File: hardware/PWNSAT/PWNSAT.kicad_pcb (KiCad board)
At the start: 2 copper layers, 83 x 83 mm, 137 parts, among them J1 Conn_01x03, J2 Conn_01x04_Pin, J3 Battery, J4 USB_A, J5 USB_A, P1 USB_C_Plug_USB2.0, Q1 DMG3415U-7, SW1 SW_Push, SW2 SW_Push, SW3 ON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

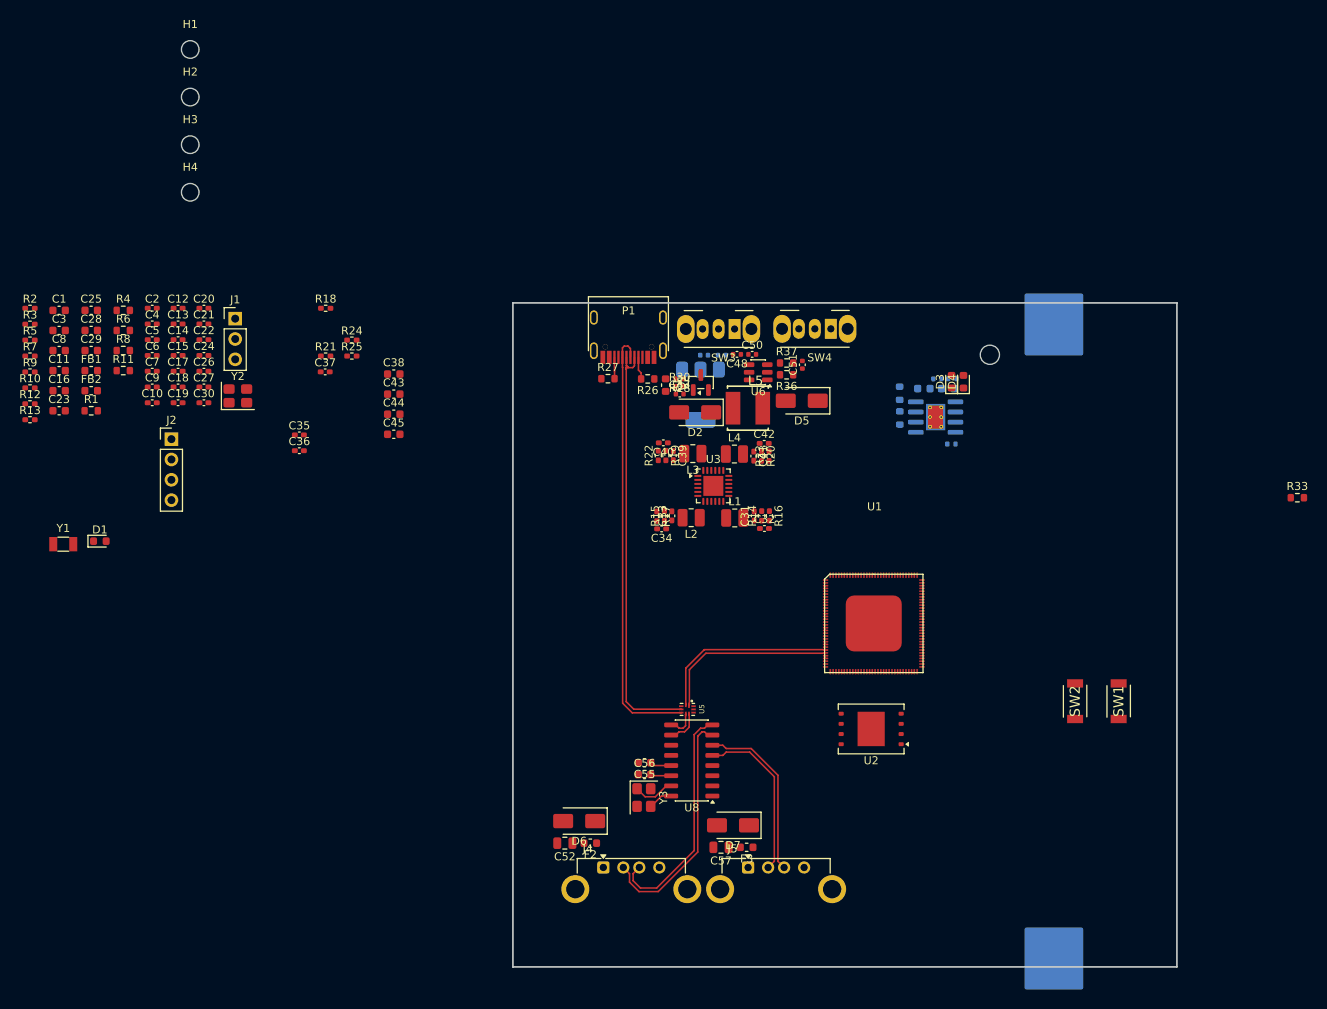
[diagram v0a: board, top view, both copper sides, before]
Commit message: feat(Hw):Update_Floorplan_Init_First _route
Pending_Battery_Type
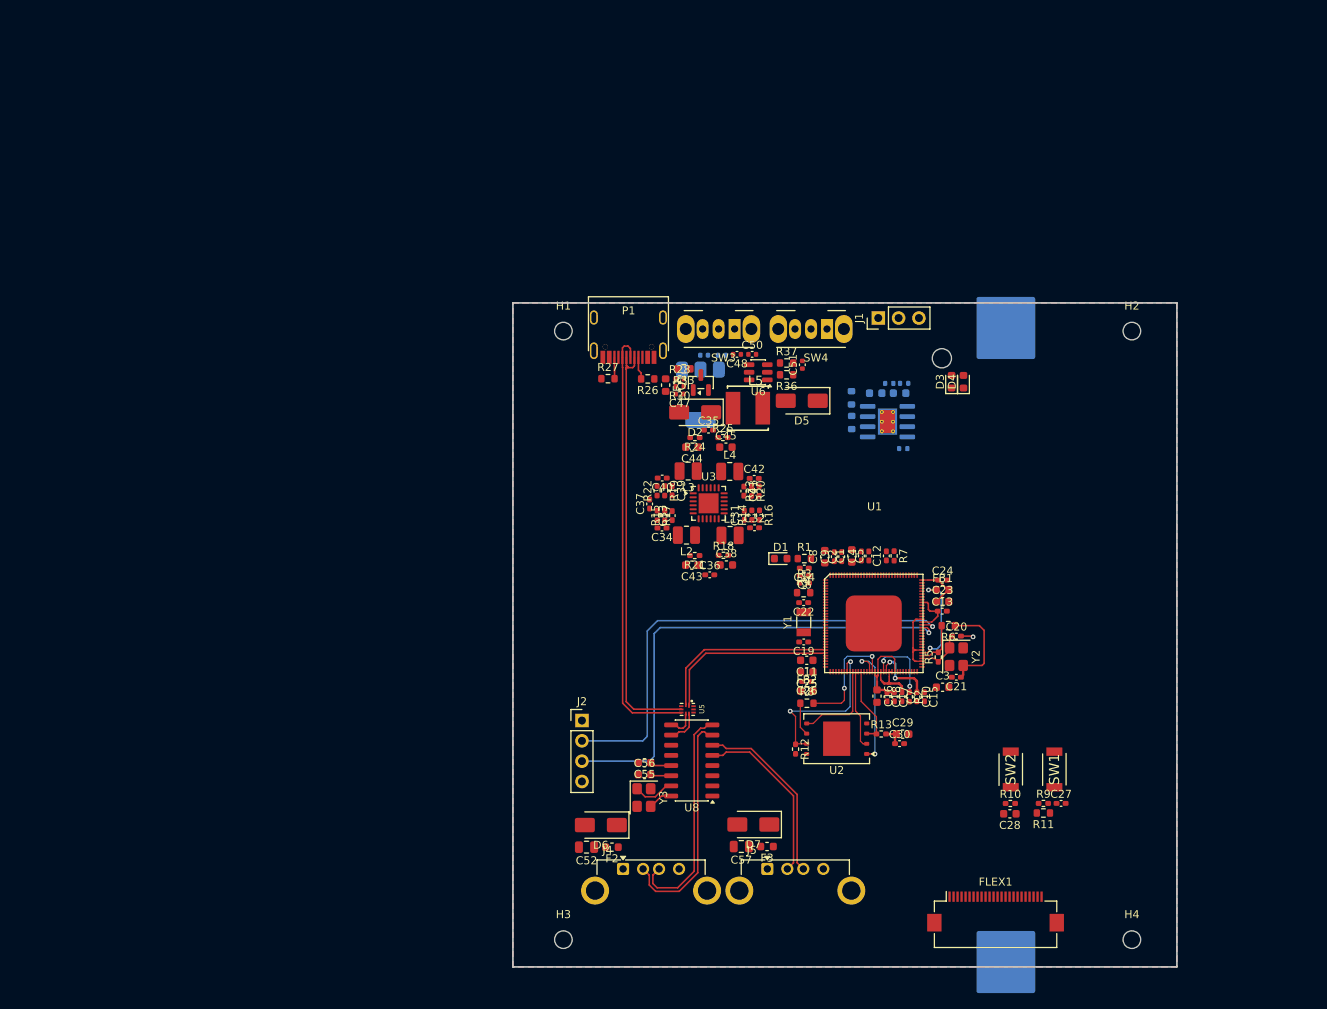
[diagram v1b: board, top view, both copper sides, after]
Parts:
- added FLEX1: FH12-24S-0.5SH(55), Connector_FFC-FPC:Hirose_FH12-24S-0.5SH_1x24-1MP_P0.50mm_Horizontal, F.Cu at (80.3, 94.2)
- moved H4 150.3 mm to (97.3, 97.7)
- moved R9 137.7 mm to (86.3, 80.7)
- moved R10 133.1 mm to (82.1, 80.7)
- moved C28 129.8 mm to (82.1, 82.0), turned to 180 degrees
- moved R11 127.6 mm to (86.3, 81.9), turned to 180 degrees
- moved H2 121.3 mm to (97.3, 21.6)
- moved R5 120.2 mm to (73.1, 62.4), turned to 90 degrees
- moved R2 120.2 mm to (69.5, 67.4), turned to -90 degrees
- moved C27 119.1 mm to (88.5, 80.7)
- moved C3 119.1 mm to (73.7, 66.2)
- moved R13 113.4 mm to (66.0, 72.0)
- moved C23 113.0 mm to (73.7, 55.5)
- moved C29 112.2 mm to (68.7, 72.0)
- moved R7 110.9 mm to (67.6, 49.8), turned to -90 degrees
- moved FB1 109.9 mm to (73.7, 54.0)
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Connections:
- SW3 pad 1: VCC -> Net-(D2-K)
- SW3 pad 2: Net-(D2-K) -> VCC
- U1 pad 31: unconnected-(U1A-CODEC_AVDD1V8-Pad31) -> /core/VCC1V8_CODEC
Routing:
- net /core/DEBUG_TX: track 0.00 -> 60.9 mm, vias 0 -> 1
- net /core/DEBUG_RX: track 0.00 -> 59.5 mm, vias 0 -> 1
- net /core/FSPI_D3: track 0.00 -> 20.7 mm, vias 0 -> 2
- net +1V8: track 0.00 -> 20.5 mm, vias 0 -> 4
- net /core/FSPI_CS0N: track 0.00 -> 15.9 mm, vias 0 -> 2
- net /core/VDD_ARM: track 0.00 -> 15.6 mm
- net Net-(U1B-EMMC_CLK/FSPI_CLK/GPIO4_B1_D): track 0.00 -> 14.7 mm, vias 0 -> 2
- net Net-(C21-Pad1): track 0.00 -> 12.3 mm
- net /core/VCC_DDR: track 0.00 -> 11.7 mm
- net /core/FSPI_D0: track 0.00 -> 11.3 mm
- net /core/FSPI_D1: track 0.00 -> 9.86 mm
- net /core/FSPI_D2: track 0.00 -> 9.82 mm
- net /core/SZQ: track 0.00 -> 9.24 mm, vias 0 -> 2
- net +3V3: track 0.00 -> 8.34 mm
- net /core/X24MIN: track 0.00 -> 6.14 mm
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- added copper zone on B.Cu, net GND
- added copper zone on F.Cu, net GND

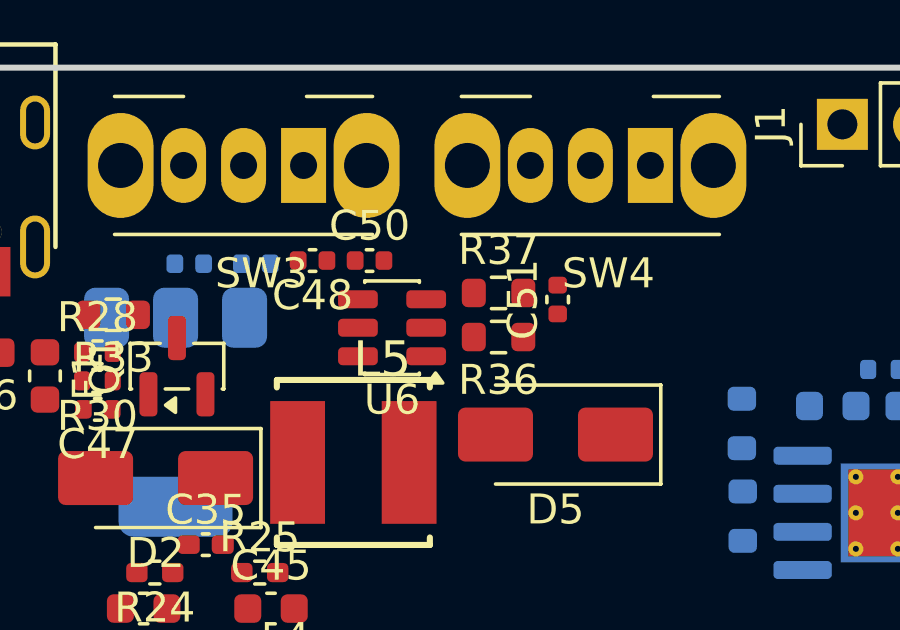
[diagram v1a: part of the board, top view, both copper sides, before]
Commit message: feat(Hw):Batt_Board_Pro_Added
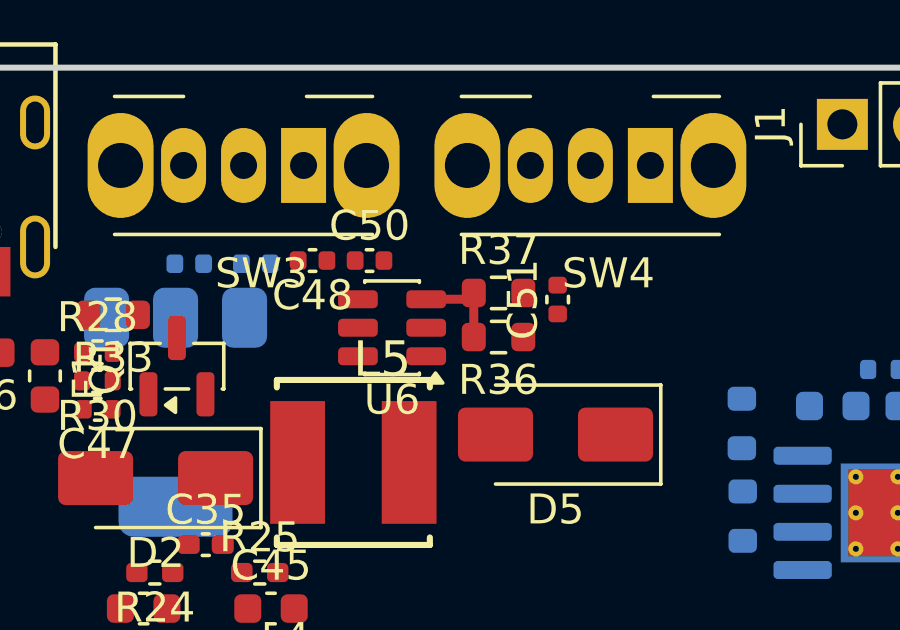
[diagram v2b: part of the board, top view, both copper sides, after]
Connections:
- FLEX1 pad 22: /Sensor/SDA_BME280 -> unconnected-(FLEX1-Pad22)
- FLEX1 pad 23: /Sensor/SCL_BME280 -> unconnected-(FLEX1-Pad23)
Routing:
- net Net-(U6-FB): track 0.00 -> 3.14 mm
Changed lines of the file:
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@@
 	(net 162 "/USB/XOUT")
 	(net 163 "unconnected-(U8-DM4-Pad1)")
+	(net 164 "unconnected-(FLEX1-Pad23)")
+	(net 165 "unconnected-(FLEX1-Pad22)")
 	(footprint "Resistor_SMD:R_0402_1005Metric_Pad0.72x0.64mm_HandSolder"
 		(layer "F.Cu")
@@
 			(size 0.3 1.3)
 			(layers "F.Cu" "F.Mask" "F.Paste")
-			(net 89 "/Sensor/SDA_BME280")
+			(net 165 "unconnected-(FLEX1-Pad22)")
 			(pinfunction "22")
 			(pintype "passive")
@@
 			(size 0.3 1.3)
 			(layers "F.Cu" "F.Mask" "F.Paste")
-			(net 127 "/Sensor/SCL_BME280")
+			(net 164 "unconnected-(FLEX1-Pad23)")
 			(pinfunction "23")
 			(pintype "passive")
@@
 	)
 	(segment
+		(start 53.335 25.64)
+		(end 53.335 27.11)
+		(width 0.3)
+		(layer "F.Cu")
+		(net 70)
+	)
+	(segment
+		(start 53.125 25.85)
+		(end 53.335 25.64)
+		(width 0.3)
+		(layer "F.Cu")
+		(net 70)
+	)
+	(segment
+		(start 51.7475 25.85)
+		(end 53.125 25.85)
+		(width 0.3)
+		(layer "F.Cu")
+		(net 70)
+	)
+	(segment

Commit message: feat(Hw):floorplans_updated
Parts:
- removed C46, C49: 10uF, Capacitor_SMD:C_0603_1608Metric
- removed C47: 100nF, Capacitor_SMD:C_0402_1005Metric
- removed C48: 10uF, Capacitor_SMD:C_0402_1005Metric
- removed D2: SS34, Diode_SMD:D_SMA
- removed D3, D4: LED, LED_SMD:LED_0603_1608Metric
- removed F1: 2A, Fuse:Fuse_0603_1608Metric
- removed FLEX1: FH12-24S-0.5SH(55), Connector_FFC-FPC:Hirose_FH12-24S-0.5SH_1x24-1MP_P0.50mm_Horizontal
- removed P1: USB_C_Plug_USB2.0, PWNCube:C393939
- removed Q1: DMG3415U-7, Package_TO_SOT_SMD:SOT-23
- removed R26, R27: 5k1, Resistor_SMD:R_0603_1608Metric
- removed R28, R29, R34: 10K, Resistor_SMD:R_0402_1005Metric
- removed R30: 18k, Resistor_SMD:R_0402_1005Metric
- removed R31, R35: 2K, Resistor_SMD:R_0603_1608Metric
- removed R32: 10.7K, Resistor_SMD:R_0402_1005Metric
- removed R33: 100K, Resistor_SMD:R_0603_1608Metric
- removed SW3: ON, Button_Switch_THT:SW_Slide_SPDT_Angled_CK_OS102011MA1Q
- removed U4: TP4056, Package_SO:SOIC-8-1EP_3.9x4.9mm_P1.27mm_EP2.41x3.3mm_ThermalVias
- added J6: Source, Connector_PinHeader_2.54mm:PinHeader_2x05_P2.54mm_Vertical, F.Cu at (42.0, 20.2)
- C53, C54, U7: moved to F.Cu
- J3: value Battery -> Sensors; footprint PWNCube:BatteryHolder_Keystone_1042_1x18650 -> Connector_PinHeader_2.54mm:PinHeader_2x20_P2.54mm_Vertical; moved to F.Cu
- moved J3 25.7 mm to (88.3, 36.0), turned to 0 degrees
- moved SW1 23.7 mm to (72.5, 94.7), turned to 90 degrees
- moved C27 19.4 mm to (71.7, 90.5), turned to 180 degrees
- moved SW2 18.8 mm to (84.0, 95.1), turned to 90 degrees
- moved R9 15.8 mm to (73.9, 90.5), turned to 180 degrees
- moved R11 14.4 mm to (73.9, 89.3), turned to 0 degrees
- moved J1 12.4 mm to (78.0, 20.5)
- moved SW4 12.1 mm to (71.3, 21.6)
- moved R10 10.3 mm to (84.1, 90.9), turned to 180 degrees
- moved C54 8.96 mm to (52.0, 20.9), turned to -90 degrees
- moved C28 7.86 mm to (84.2, 89.6), turned to 0 degrees
- moved C50 7.43 mm to (56.4, 21.0)
- moved L5 7.26 mm to (55.7, 27.8)
- moved D5 7.24 mm to (62.3, 26.8)
- moved R36 7.20 mm to (60.5, 23.6)
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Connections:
- net /USB/1_DN renamed /USB_Selector/1_DN
- net /USB/1_DP renamed /USB_Selector/1_DP
- net /USB/3_DN renamed /USB_Selector/3_DN
- net /USB/3_DP renamed /USB_Selector/3_DP
- net /USB/4_DN renamed /USB_Selector/4_DN
- net /USB/4_DP renamed /USB_Selector/4_DP
- net /USB/D+ renamed /USB_Selector/D+
- net /USB/D- renamed /USB_Selector/D-
- net /USB/S renamed /USB_Selector/S
- net /USB/SW renamed /USB_Selector/SW
- net /USB/XIN renamed /USB_Selector/XIN
- net /USB/XOUT renamed /USB_Selector/XOUT
- J3 pad 1: +BATT -> /Sensor/DIO2
- J3 pad 2: GND -> +3.3V
- U1 pad 22: /USB/Battery -> /Source_Connector/Battery
- U1 pad 25: /USB/USB_DET -> /Source_Connector/USB_DET
- U1 pad 38: unconnected-(U1B-EMMC_D5/SPI1_CLK_M0/UART1_RX_M2/I2C2_SCL_M1/GPIO4__A7_U-Pad38) -> /Sensor/R1_SCK
- U1 pad 40: unconnected-(U1B-EMMC_D4/SPI1_CS0_M0/UART1_TX_M2/I2C2_SDA_M1/GPIO4__A5_U-Pad40) -> /Sensor/R1_NSS
- U1 pad 45: unconnected-(U1B-EMMC_D6/SPI1_MOSI_M0/UART0_TX_M2/I2C0_SCL_M1/GPIO_4_A1_U-Pad45) -> /Sensor/R1_MOSI
- U1 pad 46: unconnected-(U1B-EMMC_D7/SPI1_MISO_M0/UART0_RX_M2/I2C0_SDA_M1/GPIO_4_A0_U-Pad46) -> /Sensor/R1_MISO
- U1 pad 74: /USB/Enable -> /Source_Connector/Enable
- U1 pad 83: unconnected-(U1C-VO_LCDC_D1/VI_CIF_D8_M1/PWM10_M1/UART4_RTS__M1/GPIO1_C6_D-Pad83) -> /Sensor/R1_RST
- U1 pad 84: unconnected-(U1C-VO_LCDC_D0/VI_CIF_D9_M1/PWM11_IR_M1/UART4_CT_S_M1/GPIO1_C7_D-Pad84) -> /Sensor/R1_BUSY
- U1 pad 85: unconnected-(U1C-VO_LCDC_CLK/VI_CIF_CLKO_M1/I2C3_SCL_M1/UART5__TX_M1/PWM11_IR_M2/AUD_DSM_N/GPIO1_D3_D-Pad85) -> /Sensor/R1_DIO3
- U1 pad 86: unconnected-(U1C-VO_LCDC_VSYNC/VI_CIF_VSYNC_M1/I2C3_SDA_M1/UA_RT5_RX_M1/SPI0_CS1_M0/PWM0_M1/AUD_DSM_P/GPI_O1_D2_D-Pad86) -> /Sensor/R1_DIO2
- U1 pad 87: unconnected-(U1C-VO_LCDC_HSYNC/VI_CIF_HREF_M1/PWM10_M2/UART5__CTS_M1/UART3_RX_M1/GPIO1_D1_D-Pad87) -> /Sensor/R1_DIO1
- U1 pad 89: unconnected-(U1C-VO_LCDC_DEN/VI_CIF_CLKI_M1/PWM3_IR_M2/UART5__RTS_M1/UART3_TX_M1/GPIO1_D0_D-Pad89) -> /Sensor/DIO23
- U1 pad 90: unconnected-(U1C-VO_LCDC_D2/VI_CIF_D7_M1/PWM9_M1/UART4_TX_M1/_SDMMC1_D2_M1/GPIO1_C5_D-Pad90) -> /Sensor/R1_ANT_SW
- U5 pad 4: /USB/2_DN -> /Source_Connector/2_DN
- U5 pad 5: /USB/2_DP -> /Source_Connector/2_DP
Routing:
- net /USB/2_DP: track 54.6 -> 0.00 mm
- net /Source_Connector/2_DP: track 0.00 -> 54.4 mm
- net /Source_Connector/2_DN: track 0.00 -> 53.7 mm
- net /USB/2_DN: track 52.9 -> 0.00 mm
- net Net-(C21-Pad1): track 12.3 -> 0.00 mm
- net /core/FSPI_D0: track 11.3 -> 0.00 mm
- net /core/FSPI_D1: track 9.86 -> 0.00 mm
- net /core/FSPI_D2: track 9.82 -> 0.00 mm
- net /core/VDD_ARM: track 15.6 -> 7.18 mm
- net +3V3: track 8.34 -> 0.00 mm
- net /core/X24MIN: track 6.14 -> 0.00 mm
- net /core/VCC1V8_OTP: track 6.05 -> 0.00 mm
- net /core/FSPI_D3: track 20.7 -> 14.8 mm
- net /core/X24MOUT: track 5.72 -> 0.00 mm
- net Net-(U1B-EMMC_CLK/FSPI_CLK/GPIO4_B1_D): track 14.7 -> 9.03 mm
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
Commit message: feat(Hw):PCB_PwnSat_And_Battery_Updated
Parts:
- moved FB1 6.30 mm to (69.1, 49.6), turned to 90 degrees
- moved C23 6.08 mm to (71.7, 49.7), turned to 90 degrees
- moved C24 4.41 mm to (70.5, 49.8), turned to 90 degrees
- moved R25 1.56 mm to (46.5, 36.5)
- moved R24 1.51 mm to (42.6, 36.5)
- moved C44 0.94 mm to (42.6, 35.2)
- moved C45 0.91 mm to (46.6, 35.2)
- moved C13 0.76 mm to (74.4, 56.6)
- moved L3 0.20 mm to (41.6, 39.1)
- turned C15 to 90 degrees
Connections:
- J3 pad 35: /Sensor/R1_RST -> /Sensor/R1_BUSY
- J3 pad 37: /Sensor/R1_BUSY -> /Sensor/R1_RST
- J3 pad 7: /Sensor/R0_MISO -> /Sensor/R0_MOSI
- J3 pad 9: /Sensor/R0_MOSI -> /Sensor/R0_MISO
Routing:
- net /Sensor/R1_DIO3: track 0.00 -> 46.6 mm, vias 0 -> 1
- net /USB_Selector/S: track 0.00 -> 44.7 mm, vias 0 -> 2
- net /Sensor/R1_RST: track 0.00 -> 42.0 mm, vias 0 -> 1
- net VCC: track 0.00 -> 41.3 mm
- net /Sensor/R1_DIO1: track 0.00 -> 38.2 mm, vias 0 -> 1
- net /Sensor/R1_DIO2: track 0.00 -> 37.8 mm, vias 0 -> 1
- net /Sensor/R1_BUSY: track 0.00 -> 37.3 mm, vias 0 -> 1
- net /Sensor/R0_NSS: track 0.00 -> 31.1 mm
- net /Sensor/R0_SCK: track 0.00 -> 28.7 mm
- net /Sensor/DIO23: track 0.00 -> 27.3 mm
- net /Sensor/R0_MOSI: track 0.00 -> 26.7 mm
- net /Sensor/R1_ANT_SW: track 0.00 -> 25.5 mm
- net /Sensor/R0_MISO: track 0.00 -> 24.4 mm
- net /Source_Connector/Battery: track 0.00 -> 22.7 mm
- net /core/VDD_ARM: track 7.18 -> 26.3 mm
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- added copper zone on F.Cu, net +1V8
- added copper zone on F.Cu, net +3V3
- added copper zone on F.Cu, net +5V
- added copper zone on F.Cu, net /USB_Selector/SW
- added copper zone on F.Cu, net /core/VCC_DDR
- added copper zone on F.Cu, net /core/VDD_ARM
- added copper zone on F.Cu, net /power_supply/LX1
- added copper zone on F.Cu, net /power_supply/LX2
- added copper zone on F.Cu, net /power_supply/LX3
- added copper zone on F.Cu, net /power_supply/LX4
